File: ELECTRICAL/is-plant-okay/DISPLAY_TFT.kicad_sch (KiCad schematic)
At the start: 0 parts

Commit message: feat: add header pins for tft and camera
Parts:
- added J5: PPTC111LFBN-RC, is-plant-okay-foot:CONN11_PPPN111_SUL, symbol is-plant-okay-lib:PPTC111LFBN-RC
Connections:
- new net 3.3V: J5.1
- new net GND: J5.3
- new net MISO: J5.5
- new net MOSI: J5.6
- new net SCK: J5.4
- new net TFT_BACKLIGHT: J5.11
- new net TFT_CS: J5.7
- new net TFT_DC: J5.9
- new net TFT_RST: J5.8
- new net TFT_SDCS: J5.10
- no-connect marks 0 -> 1
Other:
- note added: "adafruit tft 0.96" 160x80 breakout board datasheet: https://cdn-learn.adafruit.com/downloads/pdf/adafruit-mini-tft-0-dot-96-inch-180x60-breakout.pdf"

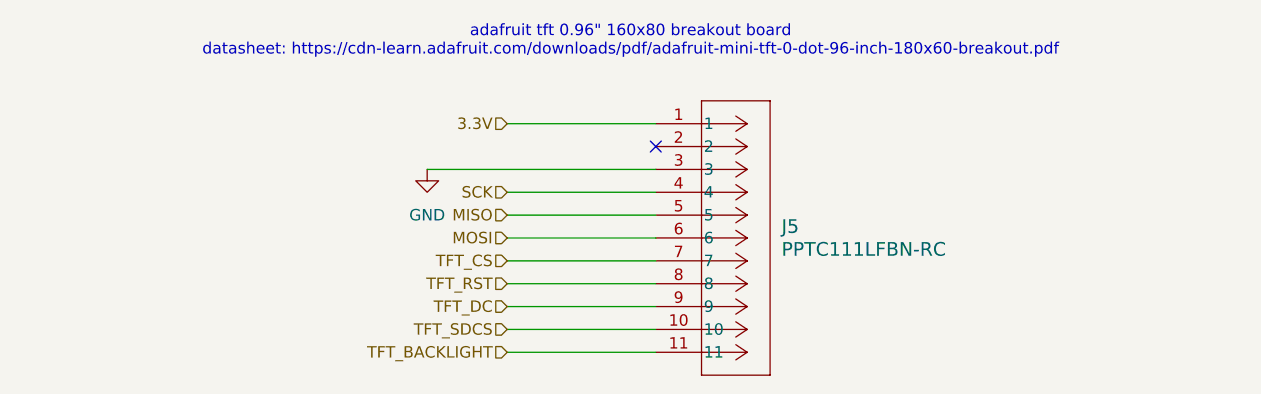
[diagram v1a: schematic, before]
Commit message: feat: add pins for mcu
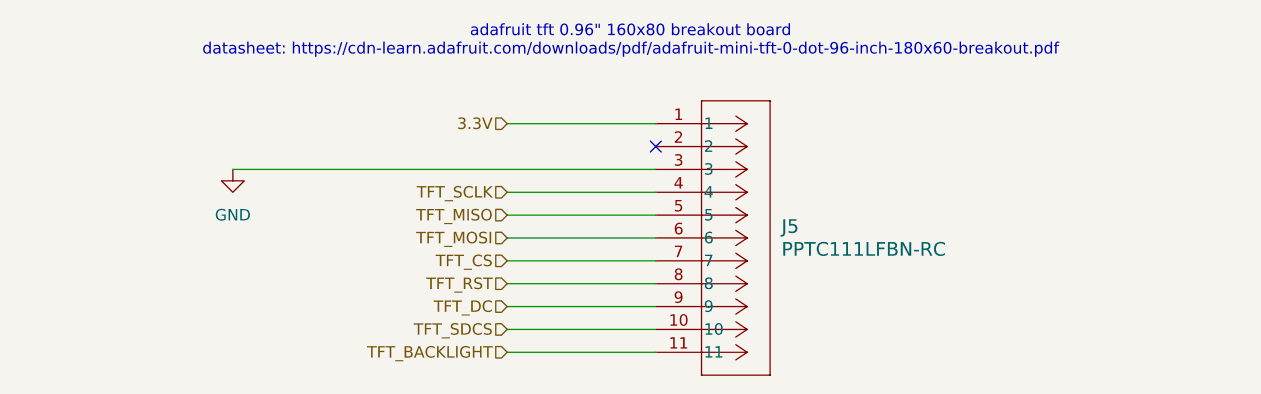
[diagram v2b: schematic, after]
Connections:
- net MISO renamed TFT_MISO
- net MOSI renamed TFT_MOSI
- net SCK renamed TFT_SCLK
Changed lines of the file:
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@@
 	(wire
 		(pts
-			(xy 109.22 83.82) (xy 134.62 83.82)
+			(xy 87.63 83.82) (xy 134.62 83.82)
 		)
 		(stroke
@@
 		)
 	)
-	(hierarchical_label "SCK"
+	(hierarchical_label "TFT_SCLK"
 		(shape input)
 		(at 118.11 86.36 180)
@@
 		)
 	)
-	(hierarchical_label "MISO"
+	(hierarchical_label "TFT_MISO"
 		(shape input)
 		(at 118.11 88.9 180)
@@
 		)
 	)
-	(hierarchical_label "MOSI"
+	(hierarchical_label "TFT_MOSI"
 		(shape input)
 		(at 118.11 91.44 180)
@@
 	(symbol
 		(lib_id "power:GND")
-		(at 109.22 83.82 0)
+		(at 87.63 83.82 0)
 		(unit 1)
 		(exclude_from_sim no)
@@
 		(fields_autoplaced yes)
 		(property "Reference" "#PWR030"
-			(at 109.22 90.17 0)
+			(at 87.63 90.17 0)
 			(effects
 				(font
@@
 		)
 		(property "Value" "GND"
-			(at 109.22 88.9 0)
+			(at 87.63 88.9 0)
 			(effects
 				(font
@@
 		)
 		(property "Footprint" ""
-			(at 109.22 83.82 0)
+			(at 87.63 83.82 0)
 			(effects
 				(font
@@
 		)
 		(property "Datasheet" ""
-			(at 109.22 83.82 0)
+			(at 87.63 83.82 0)
 			(effects
 				(font
@@
 		)
 		(property "Description" "Power symbol creates a global label with name \"GND\" , ground"
-			(at 109.22 83.82 0)
-			(effects
-				(font
+			(at 87.63 83.82 0)
+			(effects
+				(font

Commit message: feat: finished schematics
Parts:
- added TP3: TFT_3.3V_TP, TestPoint:TestPoint_Keystone_5000-5004_Miniature, symbol Connector:TestPoint
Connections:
- net 3.3V: now also TP3.1
- net TFT_RST: no longer names the net of J5.8
- no-connect marks 1 -> 2
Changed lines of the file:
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@@
 		)
+	)
+	(junction
+		(at 120.65 78.74)
+		(diameter 0)
+		(color 0 0 0 0)
 	)
 	(no_connect
 		(at 134.62 81.28)
 	)
-	(wire
-		(pts
-			(xy 118.11 96.52) (xy 134.62 96.52)
+	(no_connect
+		(at 134.62 96.52)
+	)
+	(wire
+		(pts
+			(xy 120.65 78.74) (xy 134.62 78.74)
 		)
 		(stroke
@@
 	(wire
 		(pts
-			(xy 118.11 78.74) (xy 134.62 78.74)
+			(xy 118.11 78.74) (xy 120.65 78.74)
 		)
 		(stroke
@@
 		)
 	)
-	(hierarchical_label "TFT_RST"
-		(shape input)
-		(at 118.11 96.52 180)
-		(effects
-			(font
-				(size 1.27 1.27)
-			)
-			(justify right)
-		)
-	)
 	(hierarchical_label "TFT_CS"
 		(shape input)
@@
 		)
 	)
+	(symbol
+		(lib_id "Connector:TestPoint")
+		(at 120.65 78.74 0)
+		(unit 1)
+		(exclude_from_sim no)
+		(in_bom yes)
+		(on_board yes)
+		(dnp no)
+		(fields_autoplaced yes)
+		(property "Reference" "TP3"
+			(at 123.19 74.1679 0)
+			(effects
+				(font
+					(size 1.27 1.27)
+				)
+				(justify left)
+			)
+		)
+		(property "Value" "TFT_3.3V_TP"
+			(at 123.19 76.7079 0)
+			(effects
+				(font
+					(size 1.27 1.27)
+				)
+				(justify left)
+			)
+		)
+		(property "Footprint" "TestPoint:TestPoint_Keystone_5000-5004_Miniature"
+			(at 125.73 78.74 0)
+			(effects
+				(font
+					(size 1.27 1.27)
+				)
+				(hide yes)
+			)
+		)
+		(property "Datasheet" "~"
+			(at 125.73 78.74 0)
+			(effects
+				(font
+					(size 1.27 1.27)
+				)
+				(hide yes)
+			)
+		)
+		(property "Description" "test point"
+			(at 120.65 78.74 0)
+			(effects
+				(font
+					(size 1.27 1.27)
+				)
+				(hide yes)
+			)
+		)
+		(pin "1"
+		)
+		(instances
+			(project "is-plant-okay"
+				(path "/ac51c2f9-77a4-4b89-b63f-6e0ba02b1e45/13d330f5-3cda-4311-90ba-9a1d771a2e1f"
+					(reference "TP3")
+					(unit 1)
+				)
+			)
+		)
+	)
